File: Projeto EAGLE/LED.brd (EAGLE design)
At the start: 31.8 x 21.5 mm, 8 parts, among them J1 CONECTOR, J2 CONECTOR, Q1 BC817, U1 74HC132

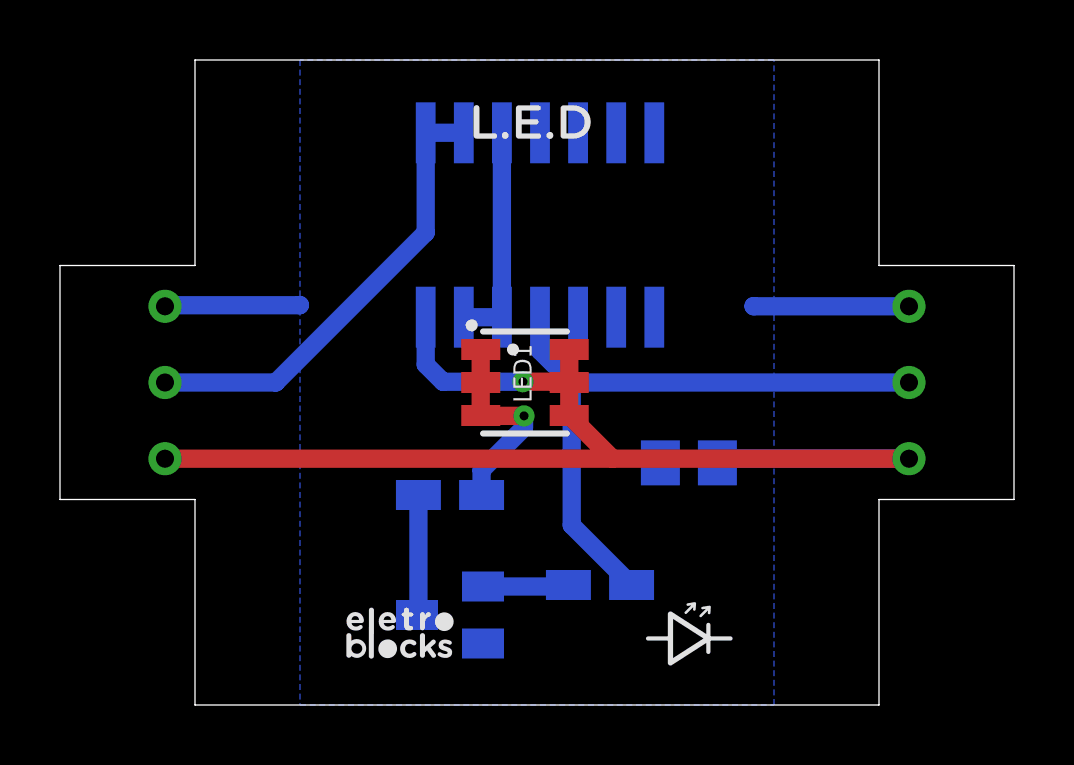
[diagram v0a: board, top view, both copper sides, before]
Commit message: correção de pads, adição de label para versionamento e plano de VCC
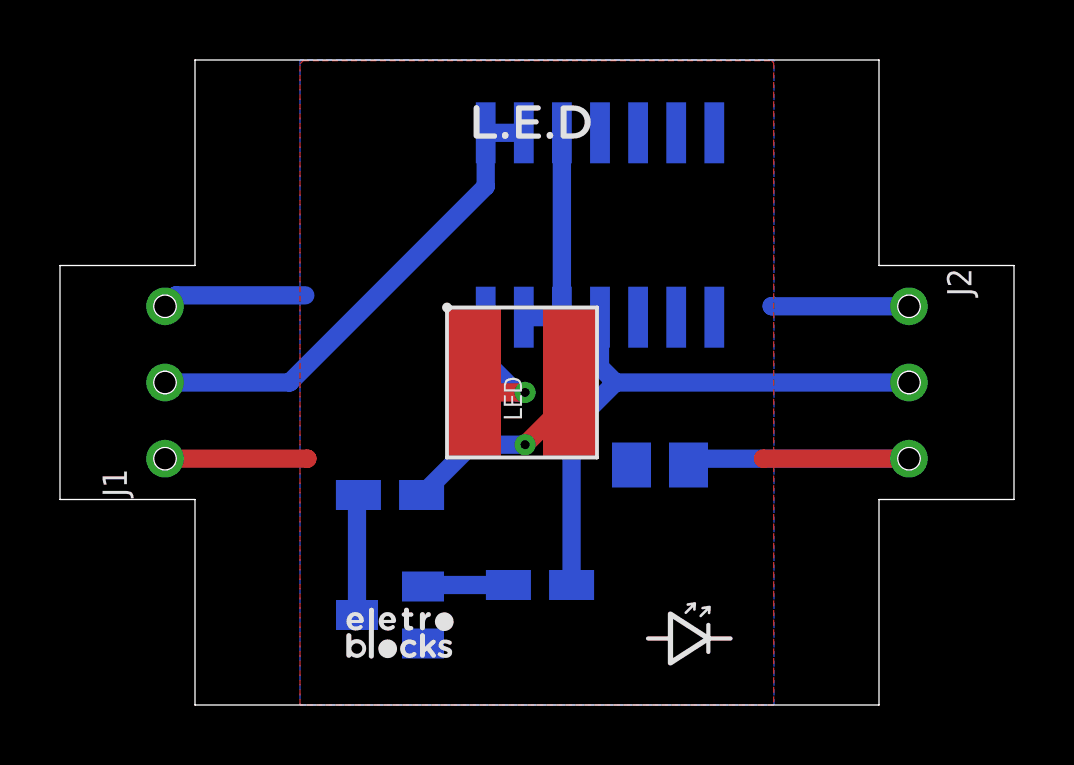
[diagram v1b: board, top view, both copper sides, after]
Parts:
- removed LED1: PLCC6PLCC-6, PLCC-6-LED:PLCC-6-LED
- added U$1: LED5050, Eletroblocks Lib:LED5050
- J1: value CONECTOR -> CONECTOR_MACHO
- J2: value CONECTOR -> CONECTOR_FEMEA
- R2: value 120R -> 150R
- moved Q1 2.00 mm to (3.00, 3.00)
- moved R1 2.00 mm to (8.00, 4.00)
- moved R2 2.00 mm to (3.00, 7.00)
- moved U1 2.00 mm to (10.0, 16.0)
- moved C1 0.97 mm to (12.0, 8.00)
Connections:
- removed net N$5: LED1.CB, LED1.CG, LED1.CR, R2.2
- new net LED: R2.2, U$1.P$2
- net VCC: now also U$1.P$1; no longer LED1.AB, LED1.AG, LED1.AR
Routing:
- net VCC: track 42.6 -> 22.1 mm
- net N$5: track 6.87 -> 0.00 mm, vias 1 -> 0
- net LED: track 0.00 -> 6.84 mm, vias 0 -> 1
- net SIGNAL_OUT: track 21.4 -> 19.5 mm
- net SIGNAL_IN: track 15.4 -> 16.5 mm
- added copper zone on layer 1, net VCC
